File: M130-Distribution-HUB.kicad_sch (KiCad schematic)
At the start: 18 parts, among them CN0 6437288-3

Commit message: Readme v1
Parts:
- F3: value 15A -> 10A
- renumbered FUEL_PUMP_RELAY_U1 to FUEL_PUMP_RELAY_U2, LIGHTS_RELAY_U1 to LIGHTS_RELAY_U4, MASTER_RELAY_U2 to MASTER_RELAY_U1, RADIATOR_FAN_RELAY_U2 to RADIATOR_FAN_RELAY_U3
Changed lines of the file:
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@@
 		(on_board yes)
 		(dnp no)
-		(property "Reference" "MASTER_RELAY_U2"
+		(property "Reference" "MASTER_RELAY_U1"
 			(at 60.198 113.284 0)
 			(effects
@@
 			(project "M130-RIFB"
 				(path "/3eed3d9c-f5f4-4289-a774-547de9333987"
-					(reference "MASTER_RELAY_U2")
+					(reference "MASTER_RELAY_U1")
 					(unit 1)
 				)
@@
 			)
 		)
-		(property "Value" "15A"
+		(property "Value" "10A"
 			(at 130.81 182.88 0)
 			(effects
@@
 		(on_board yes)
 		(dnp no)
-		(property "Reference" "LIGHTS_RELAY_U1"
+		(property "Reference" "LIGHTS_RELAY_U4"
 			(at 132.588 157.734 0)
 			(effects
@@
 			(project "M130-RIFB"
 				(path "/3eed3d9c-f5f4-4289-a774-547de9333987"
-					(reference "LIGHTS_RELAY_U1")
+					(reference "LIGHTS_RELAY_U4")
 					(unit 1)
 				)
@@
 		(on_board yes)
 		(dnp no)
-		(property "Reference" "FUEL_PUMP_RELAY_U1"
+		(property "Reference" "FUEL_PUMP_RELAY_U2"
 			(at 132.588 114.554 0)
 			(effects
@@
 			(project "M130-RIFB"
 				(path "/3eed3d9c-f5f4-4289-a774-547de9333987"
-					(reference "FUEL_PUMP_RELAY_U1")
+					(reference "FUEL_PUMP_RELAY_U2")
 					(unit 1)
 				)
@@
 		(on_board yes)
 		(dnp no)
-		(property "Reference" "RADIATOR_FAN_RELAY_U2"
+		(property "Reference" "RADIATOR_FAN_RELAY_U3"
 			(at 212.598 114.554 0)
 			(effects
@@
 			(project "M130-RIFB"
 				(path "/3eed3d9c-f5f4-4289-a774-547de9333987"
-					(reference "RADIATOR_FAN_RELAY_U2")
+					(reference "RADIATOR_FAN_RELAY_U3")
 					(unit 1)
 				)

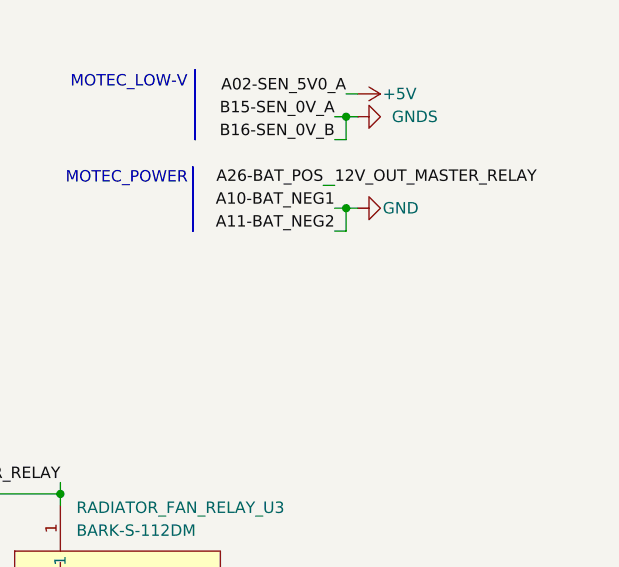
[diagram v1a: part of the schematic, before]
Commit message: Engine GND bolt
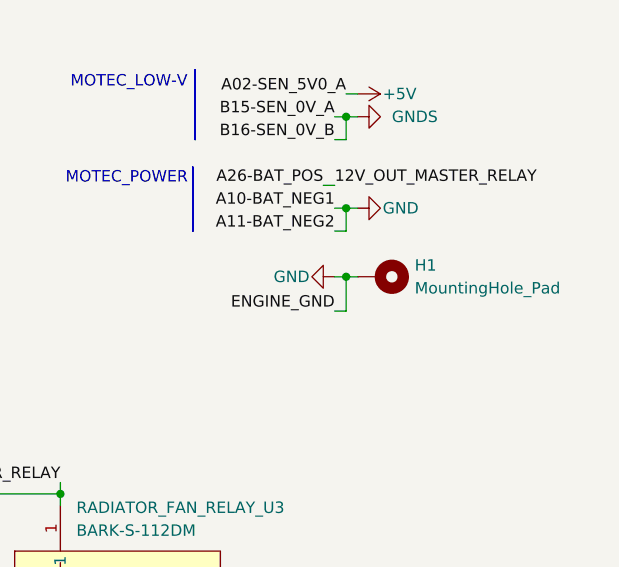
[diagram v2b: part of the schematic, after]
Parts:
- added H1: MountingHole_Pad, MountingHole:MountingHole_5.3mm_M5_DIN965_Pad_TopBottom, symbol Mechanical:MountingHole_Pad
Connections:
- net GND: now also H1.1
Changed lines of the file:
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@@
 	)
 	(junction
+		(at 242.57 88.9)
+		(diameter 0)
+		(color 0 0 0 0)
+	)
+	(junction
 		(at 242.57 71.12)
 		(diameter 0)
@@
 	(wire
 		(pts
+			(xy 241.3 88.9) (xy 242.57 88.9)
+		)
+		(stroke
+			(width 0)
+			(type default)
+		)
+	)
+	(wire
+		(pts
 			(xy 210.82 113.03) (xy 200.66 113.03)
 		)
@@
 	(wire
 		(pts
+			(xy 242.57 88.9) (xy 243.84 88.9)
+		)
+		(stroke
+			(width 0)
+			(type default)
+		)
+	)
+	(wire
+		(pts
 			(xy 121.92 81.28) (xy 121.92 82.55)
 		)
@@
 	(wire
 		(pts
+			(xy 242.57 88.9) (xy 242.57 92.71)
+		)
+		(stroke
+			(width 0)
+			(type default)
+		)
+	)
+	(wire
+		(pts
 			(xy 241.3 81.28) (xy 242.57 81.28)
 		)
@@
 		)
 	)
+	(wire
+		(pts
+			(xy 242.57 92.71) (xy 241.3 92.71)
+		)
+		(stroke
+			(width 0)
+			(type default)
+		)
+	)
 	(label "A18-OUT_HB1"
 		(at 59.69 48.26 0)
@@
 		)
 	)
+	(label "ENGINE_GND"
+		(at 241.3 92.71 180)
+		(effects
+			(font
+				(size 1.27 1.27)
+			)
+			(justify right bottom)
+		)
+	)
 	(label "B26-ETH_RX-"
 		(at 237.49 31.75 180)
@@
 	)
 	(symbol
+		(lib_id "Mechanical:MountingHole_Pad")
+		(at 246.38 88.9 270)
+		(unit 1)
+		(exclude_from_sim no)
+		(in_bom no)
+		(on_board yes)
+		(dnp no)
+		(fields_autoplaced yes)
+		(property "Reference" "H1"
+			(at 250.19 87.6299 90)
+			(effects
+				(font
+					(size 1.27 1.27)
+				)
+				(justify left)
+			)
+		)
+		(property "Value" "MountingHole_Pad"
+			(at 250.19 90.1699 90)
+			(effects
+				(font
+					(size 1.27 1.27)
+				)
+				(justify left)
+			)
+		)
+		(property "Footprint" "MountingHole:MountingHole_5.3mm_M5_DIN965_Pad_TopBottom"
+			(at 246.38 88.9 0)
+			(effects
+				(font
+					(size 1.27 1.27)
+				)
+				(hide yes)
+			)
+		)
+		(property "Datasheet" "~"
+			(at 246.38 88.9 0)
+			(effects
+				(font
+					(size 1.27 1.27)
+				)
+				(hide yes)
+			)
+		)
+		(property "Description" "Mounting Hole with connection"
+			(at 246.38 88.9 0)
+			(effects
+				(font
+					(size 1.27 1.27)
+				)
+				(hide yes)
+			)
+		)
+		(pin "1"
+		)
+		(instances
+			(project ""
+				(path "/3eed3d9c-f5f4-4289-a774-547de9333987"
+					(reference "H1")
+					(unit 1)
+				)
+			)
+		)
+	)
+	(symbol
 		(lib_id "power:GND")
 		(at 173.99 22.86 270)
@@
 					(unit 1)
 				)
+			)
+		)
+	)
+	(symbol
+		(lib_id "power:GND")
+		(at 241.3 88.9 270)
+		(unit 1)
+		(exclude_from_sim no)
+		(in_bom yes)
+		(on_board yes)
+		(dnp no)
+		(property "Reference" "#PWR024"
+			(at 234.95 88.9 0)
+			(effects
+				(font
+					(size 1.27 1.27)
+				)
+				(hide yes)
+			)
+		)
+		(property "Value" "GND"
+			(at 238.506 88.9 90)
+			(effects
+				(font
+					(size 1.27 1.27)
+				)
+				(justify right)
+			)
+		)
+		(property "Footprint" ""
+			(at 241.3 88.9 0)
+			(effects
+				(font
+					(size 1.27 1.27)
+				)
+				(hide yes)
+			)
+		)
+		(property "Datasheet" ""
+			(at 241.3 88.9 0)
+			(effects
+				(font
+					(size 1.27 1.27)
+				)
+				(hide yes)
+			)
+		)
+		(property "Description" "Power symbol creates a global label with name \"GND\" , ground"
+			(at 241.3 88.9 0)
+			(effects
+				(font
+					(size 1.27 1.27)
+				)
+				(hide yes)
+			)
+		)
+		(pin "1"
+		)
+		(instances
+			(project "M130-Distribution-HUB"
+				(path "/3eed3d9c-f5f4-4289-a774-547de9333987"
+					(reference "#PWR024")
+					(unit 1)
+				)

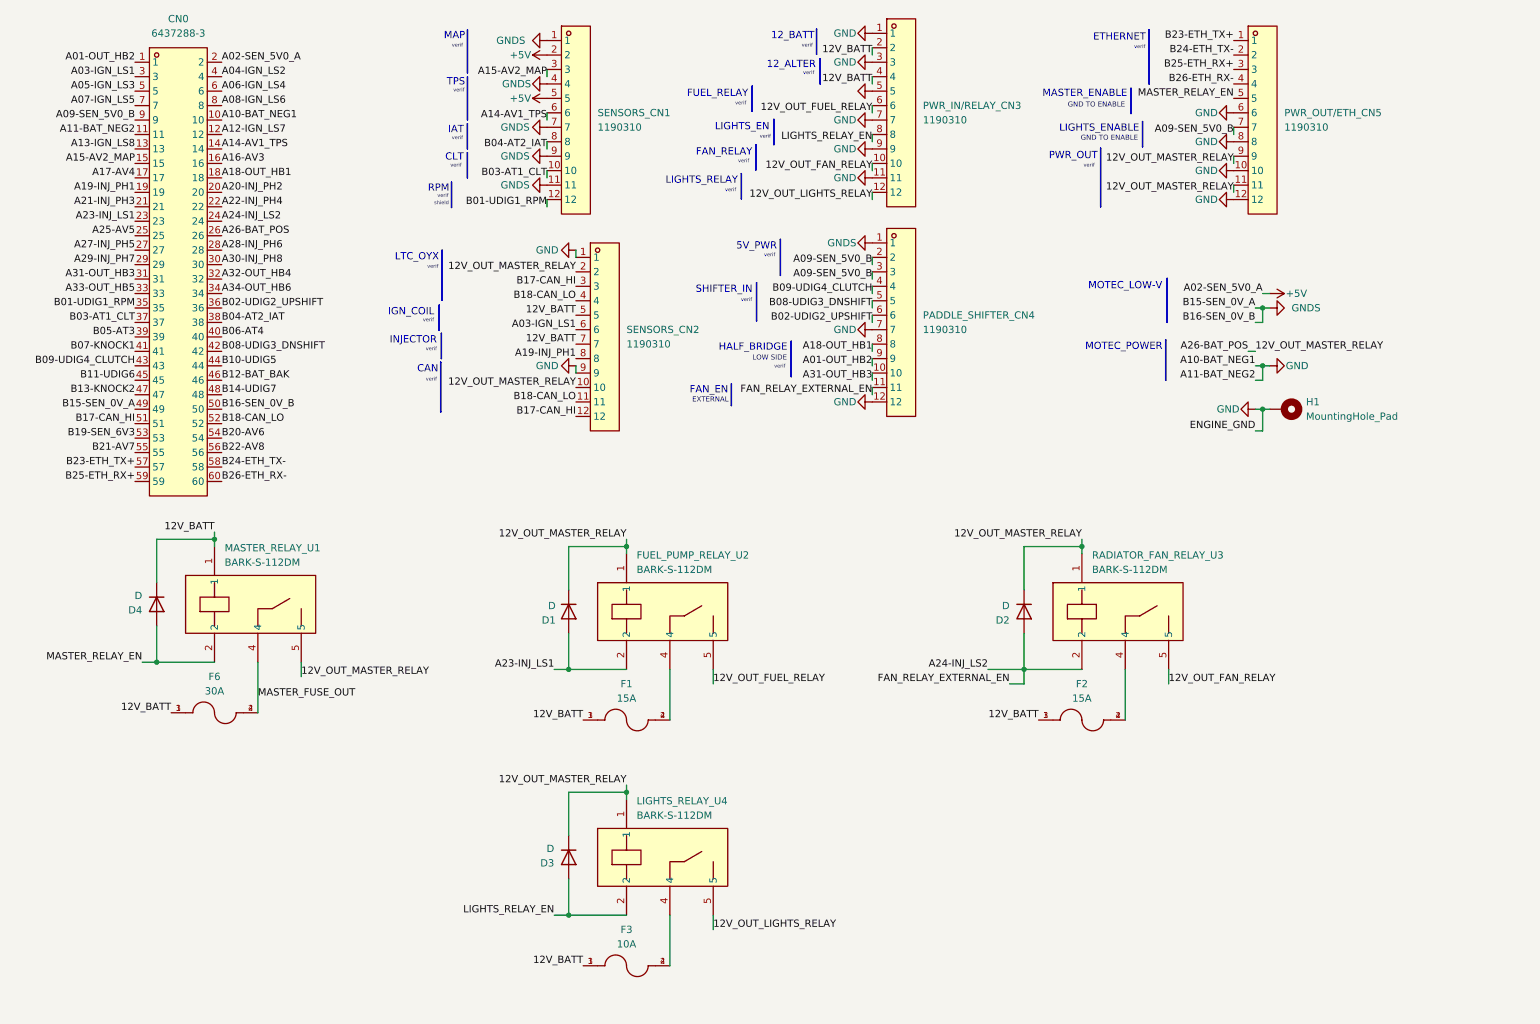
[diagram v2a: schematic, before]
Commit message: Thermal relif
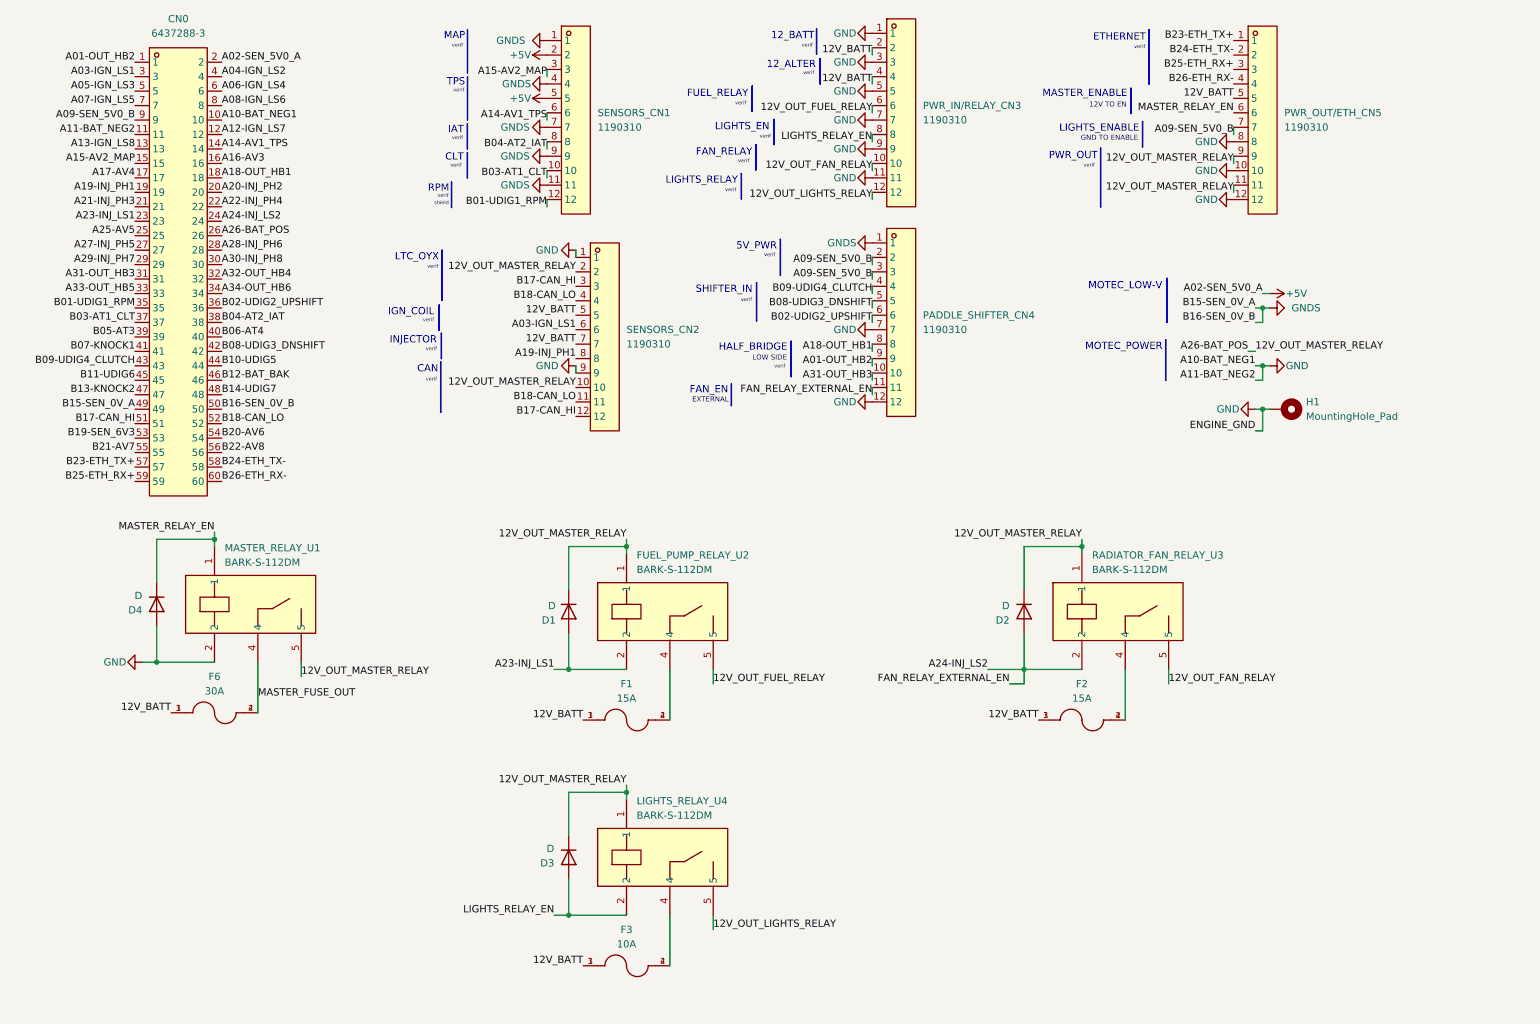
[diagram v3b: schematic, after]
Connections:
- net 12V_BATT: now also PWR_OUT/ETH_CN5.5; no longer D4.1 (K), MASTER_RELAY_U1.1
- net GND: now also D4.2 (A), MASTER_RELAY_U1.2; no longer PWR_OUT/ETH_CN5.6
- net MASTER_RELAY_EN: now also D4.1 (K), MASTER_RELAY_U1.1, PWR_OUT/ETH_CN5.6; no longer D4.2 (A), MASTER_RELAY_U1.2, PWR_OUT/ETH_CN5.5
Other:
- note added: "12V TO EN"
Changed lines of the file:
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@@
 		)
 	)
-	(text "GND TO ENABLE"
+	(text "12V TO EN"
 		(exclude_from_sim no)
-		(at 213.36 35.56 0)
+		(at 215.392 35.56 0)
 		(effects
 			(font
@@
 		)
 	)
-	(label "MASTER_RELAY_EN"
-		(at 237.49 34.29 180)
-		(effects
-			(font
-				(size 1.27 1.27)
-			)
-			(justify right bottom)
-		)
-	)
 	(label "A23-INJ_LS1"
 		(at 44.45 55.88 180)
@@
 		)
 	)
+	(label "MASTER_RELAY_EN"
+		(at 237.49 36.83 180)
+		(effects
+			(font
+				(size 1.27 1.27)
+			)
+			(justify right bottom)
+		)
+	)
 	(label "B21-AV7"
 		(at 44.45 96.52 180)
@@
 		)
 	)
+	(label "MASTER_RELAY_EN"
+		(at 58.42 110.49 180)
+		(effects
+			(font
+				(size 1.27 1.27)
+			)
+			(justify right bottom)
+		)
+	)
 	(label "A01-OUT_HB2"
 		(at 44.45 27.94 180)
@@
 	)
 	(label "12V_BATT"
-		(at 58.42 110.49 180)
+		(at 237.49 34.29 180)
 		(effects
 			(font
@@
 		)
 	)
-	(label "MASTER_RELAY_EN"
-		(at 45.72 133.35 180)
-		(effects
-			(font
-				(size 1.27 1.27)
-			)
-			(justify right bottom)
-		)
-	)
 	(label "12V_OUT_MASTER_RELAY"
 		(at 241.3 78.74 0)
@@
 				)
 				(justify right)
-				(hide yes)
 			)
 		)
@@
 	)
 	(symbol
+		(lib_id "power:GND")
+		(at 45.72 133.35 270)
+		(unit 1)
+		(exclude_from_sim no)
+		(in_bom yes)
+		(on_board yes)
+		(dnp no)
+		(property "Reference" "#PWR025"
+			(at 39.37 133.35 0)
+			(effects
+				(font
+					(size 1.27 1.27)
+				)
+				(hide yes)
+			)
+		)
+		(property "Value" "GND"
+			(at 42.926 133.35 90)
+			(effects
+				(font
+					(size 1.27 1.27)
+				)
+				(justify right)
+			)
+		)
+		(property "Footprint" ""
+			(at 45.72 133.35 0)
+			(effects
+				(font
+					(size 1.27 1.27)
+				)
+				(hide yes)
+			)
+		)
+		(property "Datasheet" ""
+			(at 45.72 133.35 0)
+			(effects
+				(font
+					(size 1.27 1.27)
+				)
+				(hide yes)
+			)
+		)
+		(property "Description" "Power symbol creates a global label with name \"GND\" , ground"
+			(at 45.72 133.35 0)
+			(effects
+				(font
+					(size 1.27 1.27)
+				)
+				(hide yes)
+			)
+		)
+		(pin "1"
+		)
+		(instances
+			(project "M130-Distribution-HUB"
+				(path "/3eed3d9c-f5f4-4289-a774-547de9333987"
+					(reference "#PWR025")
+					(unit 1)
+				)
+			)
+		)
+	)
+	(symbol
 		(lib_id "EasyEDA:BARK-S-112DM")
 		(at 218.44 124.46 0)
@@
 					(unit 1)
 				)
-			)
-		)
-	)
-	(symbol
-		(lib_id "power:GND")
-		(at 237.49 36.83 270)
-		(unit 1)
-		(exclude_from_sim no)
-		(in_bom yes)
-		(on_board yes)
-		(dnp no)
-		(property "Reference" "#PWR011"
-			(at 231.14 36.83 0)
-			(effects
-				(font
-					(size 1.27 1.27)
-				)
-				(hide yes)
-			)
-		)
-		(property "Value" "GND"
-			(at 234.696 36.83 90)
-			(effects
-				(font
-					(size 1.27 1.27)
-				)
-				(justify right)
-			)
-		)
-		(property "Footprint" ""
-			(at 237.49 36.83 0)
-			(effects
-				(font
-					(size 1.27 1.27)
-				)
-				(hide yes)
-			)
-		)
-		(property "Datasheet" ""
-			(at 237.49 36.83 0)
-			(effects
-				(font
-					(size 1.27 1.27)
-				)
-				(hide yes)
-			)
-		)
-		(property "Description" "Power symbol creates a global label with name \"GND\" , ground"
-			(at 237.49 36.83 0)
-			(effects
-				(font
-					(size 1.27 1.27)
-				)
-				(hide yes)
-			)
-		)
-		(pin "1"
-		)
-		(instances
-			(project "M130-RIFB"
-				(path "/3eed3d9c-f5f4-4289-a774-547de9333987"
-					(reference "#PWR011")
-					(unit 1)
-				)

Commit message: Moved to vertical connectors
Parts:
- PADDLE_SHIFTER_CN4, PWR_IN/RELAY_CN3, PWR_OUT/ETH_CN5, SENSORS_CN1, SENSORS_CN2: value 1190310 -> 1991192; footprint EasyEDA:CONN-TH_12P-P5.00_1190310 -> EasyEDA:PHOENIX_1991192
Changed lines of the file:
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@@
 		(fields_autoplaced yes)
 		(property "Reference" "PWR_IN/RELAY_CN3"
-			(at 182.88 35.5599 0)
+			(at 182.88 35.56 0)
 			(effects
 				(font
@@
 			)
 		)
-		(property "Value" "1190310"
-			(at 182.88 38.0999 0)
+		(property "Value" "1991192"
+			(at 182.88 38.1 0)
 			(effects
 				(font
@@
 			)
 		)
-		(property "Footprint" "EasyEDA:CONN-TH_12P-P5.00_1190310"
+		(property "Footprint" "EasyEDA:PHOENIX_1991192"
 			(at 179.07 58.42 0)
 			(effects
@@
 		(fields_autoplaced yes)
 		(property "Reference" "SENSORS_CN1"
-			(at 125.73 36.8299 0)
+			(at 125.73 36.83 0)
 			(effects
 				(font
@@
 			)
 		)
-		(property "Value" "1190310"
-			(at 125.73 39.3699 0)
+		(property "Value" "1991192"
+			(at 125.73 39.37 0)
 			(effects
 				(font
@@
 			)
 		)
-		(property "Footprint" "EasyEDA:CONN-TH_12P-P5.00_1190310"
+		(property "Footprint" "EasyEDA:PHOENIX_1991192"
 			(at 121.92 59.69 0)
 			(effects
@@
 		(fields_autoplaced yes)
 		(property "Reference" "PADDLE_SHIFTER_CN4"
-			(at 182.88 72.3899 0)
+			(at 182.88 72.39 0)
 			(effects
 				(font
@@
 			)
 		)
-		(property "Value" "1190310"
-			(at 182.88 74.9299 0)
+		(property "Value" "1991192"
+			(at 182.88 74.93 0)
 			(effects
 				(font
@@
 			)
 		)
-		(property "Footprint" "EasyEDA:CONN-TH_12P-P5.00_1190310"
+		(property "Footprint" "EasyEDA:PHOENIX_1991192"
 			(at 179.07 95.25 0)
 			(effects
@@
 		(fields_autoplaced yes)
 		(property "Reference" "SENSORS_CN2"
-			(at 130.81 74.9299 0)
+			(at 130.81 74.93 0)
 			(effects
 				(font
@@
 			)
 		)
-		(property "Value" "1190310"
-			(at 130.81 77.4699 0)
+		(property "Value" "1991192"
+			(at 130.81 77.47 0)
 			(effects
 				(font
@@
 			)
 		)
-		(property "Footprint" "EasyEDA:CONN-TH_12P-P5.00_1190310"
+		(property "Footprint" "EasyEDA:PHOENIX_1991192"
 			(at 127 97.79 0)
 			(effects
@@
 		(fields_autoplaced yes)
 		(property "Reference" "PWR_OUT/ETH_CN5"
-			(at 246.38 36.8299 0)
+			(at 246.38 36.83 0)
 			(effects
 				(font
@@
 			)
 		)
-		(property "Value" "1190310"
-			(at 246.38 39.3699 0)
+		(property "Value" "1991192"
+			(at 246.38 39.37 0)
 			(effects
 				(font
@@
 			)
 		)
-		(property "Footprint" "EasyEDA:CONN-TH_12P-P5.00_1190310"
+		(property "Footprint" "EasyEDA:PHOENIX_1991192"
 			(at 242.57 59.69 0)
 			(effects

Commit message: Slight changes
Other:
- note added: "Designed by: Isaac Subudhi"
- note added: "M130-Distribution-HUB"
- note added: "Wed, Feb, 4th"
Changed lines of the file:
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@@
+		)
+	)
+	(text "Wed, Feb, 4th"
+		(exclude_from_sim no)
+		(at 211.074 193.802 0)
+		(effects
+			(font
+				(size 1.27 1.27)
+			)
 		)
 	)
@@
 		)
 	)
+	(text "Designed by: Isaac Subudhi"
+		(exclude_from_sim no)
+		(at 273.304 189.992 0)
+		(effects
+			(font
+				(size 1.27 1.27)
+			)
+		)
+	)
 	(text "verif"
 		(exclude_from_sim no)
@@
 		(effects
 			(font
+				(size 1.27 1.27)
+			)
+		)
+	)
+	(text "M130-Distribution-HUB"
+		(exclude_from_sim no)
+		(at 194.818 189.992 0)
+		(effects
+			(font
